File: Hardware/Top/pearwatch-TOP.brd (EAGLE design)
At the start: 38 x 38 mm, 49 parts, among them U2 NRF52832_MODULE_MDBT42, U4 PCF8523

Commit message: adding updated top board
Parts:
- added SW1, SW2: SWITCH.MOM, LinnesLab-Switches:TACTILE_SWITCH_SMD_6.2MM_TALL
- moved LDO2 9.76 mm to (9.45, 9.14)
- moved D5 7.69 mm to (3.38, 7.21)
- moved R15 7.57 mm to (17.8, 9.45)
- moved D4 7.44 mm to (3.45, 8.97)
- moved C6 7.39 mm to (15.8, 9.25)
- moved C5 5.79 mm to (12.5, 8.92), turned to 180 degrees
- moved R12 5.43 mm to (13.2, 10.3)
- moved C20 4.28 mm to (11.3, 12.7)
- moved R14 4.02 mm to (6.60, 8.43)
- moved CHRG2 3.69 mm to (14.8, 12.5)
- moved R13 1.58 mm to (8.94, 12.5)
- moved C21 1.49 mm to (19.6, 11.0)
- moved R11 1.42 mm to (18.5, 13.2)
- moved XTAL3 0.77 mm to (3.40, 29.4)
- moved R7 0.74 mm to (6.02, 10.7)
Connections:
- net GND: now also USB2.S1, USB2.S2, USB2.S3, USB2.S4, USB2.S5, USB2.S6
- net N$5: now also C14.2, D1.+, R5.1
- net RESET: no longer C14.2, D1.+, R5.1

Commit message: updating top board
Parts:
- removed C10, C11: 300p, LinnesLab-Passives:C0603
- removed C12: 10u, LinnesLab-Passives:C0805
- removed C13, C15, C17, C18, C19: 2.2uF, LinnesLab-Passives:C0402
- removed C14: 100n, LinnesLab-Passives:C0603
- removed C16: 10uF, LinnesLab-Passives:C0603
- removed CORTEX1: CORTEX_DEBUG_PTH, LinnesLab-Connectors:2X5-PTH-1.27MM
- removed D1: (no value), LinnesLab-DiscreteSemi:USC
- removed L2: 10u, LinnesLab-Passives:L0603
- removed SW3, SW4: (no value), LinnesLab-Switches:BUTTON-GULLWING
- removed U4: PCF8523, LinnesLab-Clocks:SO8
- removed XTAL3: 32.7680kHz, LinnesLab-Clocks:2-SMD.NOLEAD.2.0MMTO1.2MM
- added C25, C33, C35, C36, C37: 2.2uF, LinnesLab-Passives:C0402
- added C26: 1u, LinnesLab-Passives:C0603
- added C27, C28: (no value), LinnesLab-Passives:C0603
- added C29, C30: 300p, LinnesLab-Passives:C0603
- added C31: 10u, LinnesLab-Passives:C0805
- added C32: 100n, LinnesLab-Passives:C0603
- added C34: 10uF, LinnesLab-Passives:C0603
- added CORTEX3: CORTEX_DEBUG_PTH, LinnesLab-Connectors:2X5-PTH-1.27MM
- added D3: (no value), LinnesLab-DiscreteSemi:USC
- added JP2: (no value), LinnesLab-Switches:SMT-JUMPER_2_NO_SILK
- added L3: 10u, LinnesLab-Passives:L0603
- added LED5: RED, LinnesLab-LED:LED-0603
- added LED6: BLUE, LinnesLab-LED:LED-0603
- added R10, R18: 10k, LinnesLab-Passives:R0603
- added R16, R17, R20: 1k, LinnesLab-Passives:R0603
- added R19: 390k, LinnesLab-Passives:R0603
- added R21, R22: (no value), LinnesLab-Passives:R0603
- added SW7, SW8: (no value), LinnesLab-Switches:BUTTON-GULLWING
- added U5: NRF52832_MODULE_MDBT42, LinnesLab-Microcontrollers:BLE_MODULE_RAYTAC_MDBT42
- added U6: (no value), LinnesLab-Displays:UG-2864HSWEG01_0.96IN_NO-WRAPAROUND
- added XTAL4: 32.768kHz, LinnesLab-Clocks:2-SMD.NOLEAD.2.0MMTO1.2MM
- C7: value 1u -> 100n
- C8, C9: value (none) -> 47p
- LED4: value BLUE -> YELLOW
- R3, R4: value 1k -> 10k
- R5, R6: value 10k -> 27
- R7: value 390k -> 1k
- R8, R9: value 10k -> 10K
- U2: value NRF52832_MODULE_MDBT42 -> FT231XS; device LinnesLab-Microcontrollers:BLE_MODULE_RAYTAC_MDBT42 -> LinnesLab-DigitalIC:SSOP20_L
- U3: value (none) -> PCF8523; device LinnesLab-Displays:UG-2864HSWEG01_0.96IN_NO-WRAPAROUND -> LinnesLab-Clocks:SO8
- XTAL2: value 32.768kHz -> 32.7680kHz
- moved R7 72.8 mm to (77.6, -2.57)
- moved C7 54.1 mm to (73.8, 5.31), turned to 0 degrees
- moved C8 50.8 mm to (73.8, 0.23)
- moved C9 48.9 mm to (73.8, -4.85)
- moved LED4 43.7 mm to (77.6, 1.24)
- moved R5 41.2 mm to (6.27, 4.55), turned to 0 degrees
- moved LED3 40.5 mm to (77.6, 5.05)
- moved XTAL2 28.5 mm to (2.13, 30.6), turned to 90 degrees
- moved R8 27.0 mm to (29.5, 5.77), turned to 0 degrees
- moved R9 27.0 mm to (29.5, 3.07), turned to 0 degrees
- moved R4 25.9 mm to (13.4, 25.4), turned to 90 degrees
- moved R3 25.6 mm to (13.4, 28.8), turned to 90 degrees
- moved U3 14.7 mm to (3.68, 24.6)
- moved R6 10.4 mm to (5.46, 2.31)
- moved U2 9.84 mm to (21.5, 25.7), turned to 270 degrees
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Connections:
- removed net N$10: LED4.A, R4.1
- removed net N$11: L2.1, U2.10
- removed net N$12: C7.1, L2.2, U2.9
- removed net N$13: C16.2, U3.28
- removed net N$14: CORTEX1.8
- removed net N$15: C18.2, U3.27
- removed net N$19: U4.2, XTAL3.P$1
- removed net N$20: U4.1, XTAL3.P$2
- removed net N$4: C8.2, U2.13, XTAL2.P$1
- removed net N$5: C13.1, C14.2, D1.+, R5.1, U3.3
- removed net N$9: LED3.A, R3.1
- removed net RXD: U2.21
- removed net TXD: U2.19
- new net !CTS: JP2.2, U2.9
- new net !DTR: U2.1
- new net FT3V3: U2.13
- new net N$18: R10.2, U6.11
- new net N$21: R19.1, U6.26
- new net N$23: C25.2, U6.2
- new net N$26: C27.2, U5.13, XTAL4.P$1
- new net N$27: C28.1, U5.14, XTAL4.P$2
- new net N$28: LED5.A, R16.1
- new net N$29: LED6.A, R17.1
- new net N$30: L3.1, U5.10
- new net N$31: C26.1, L3.2, U5.9
- new net N$32: CORTEX3.8
- new net N$33: C25.1, U6.3
- new net N$34: C33.2, U6.4
- new net N$35: C33.1, U6.5
- new net N$36: C34.2, U6.28
- new net N$37: C36.2, U6.27
- new net RXD.FT: U2.4
- new net RXD.NRF: R21.2, U5.21
- new net RXDFT: R22.1
- new net RXLED: R7.1, U2.17
- new net TXD.FT: R21.1, U2.20
- new net TXD.NRF: R22.2, U5.19
- new net TXLED: R20.1, U2.10
- net 3.3V: now also C31.2, C35.2, C37.2, C7.2, CORTEX3.1, D3.-, LED3.A, LED4.A, R18.2, R3.2, R4.2, U2.14, U2.3, U3.8, U5.11, U6.6, U6.9; no longer C12.2, C17.2, C19.2, CORTEX1.1, D1.-, R5.2, U2.11, U3.6, U3.9, U4.8
- net CS.OLED: now also U6.13; no longer U3.13
- net DC.OLED: now also U6.15; no longer U3.15
- net DFU: now also SW7.3, U5.34; no longer SW3.3, U2.34
- net DTR: now also C32.1; no longer C14.1
- net FRST: now also U5.38; no longer U2.38
- net GND: now also C26.2, C27.1, C28.2, C29.2, C30.2, C31.1, C34.1, C35.1, C36.1, C37.1, C7.1, C8.2, C9.1, CORTEX3.3, CORTEX3.5, CORTEX3.7, CORTEX3.9, JP2.1, LED5.C, LED6.C, R10.1, R19.2, SW7.1, SW8.3, U2.16, U2.6, U3.4, U5.1, U5.12, U5.24, U5.39, U6.1, U6.10, U6.12, U6.29, U6.30, U6.8; no longer C10.2, C11.2, C12.1, C16.1, C17.1, C18.1, C19.1, C7.2, C8.1, C9.2, CORTEX1.3, CORTEX1.5, CORTEX1.7, CORTEX1.9, LED3.C, LED4.C, R6.1, R7.2, SW3.1, SW4.3, U2.1, U2.12, U2.24, U2.39, U3.1, U3.10, U3.12, U3.29, U3.30, U3.8, U4.4
- net LED1: now also R16.2, U5.31; no longer R3.2, U2.31
- net LED2: now also R17.2, U5.33; no longer R4.2, U2.33
- net MISO: now also U5.28; no longer U2.28
- net MOSI: now also U5.27, U6.19; no longer U2.27, U3.19
- net N$1: now also U3.2, XTAL2.P$1; no longer R6.2, U3.11
- net N$2: now also U3.1, XTAL2.P$2; no longer R7.1, U3.26
- net N$3: now also R5.2, U2.12; no longer C13.2, U3.2
- net N$6: now also R6.2, U2.11; no longer C9.1, U2.14, XTAL2.P$2
- net N$7: now also LED3.C, R7.2; no longer C15.2, U3.4
- net N$8: now also LED4.C, R20.2; no longer C15.1, U3.5
- net P0.09/NFC1: now also C30.1, U5.22; no longer C11.1, U2.22
- net P0.10/NFC2: now also C29.1, U5.23; no longer C10.1, U2.23
- net RESET: now also C32.2, CORTEX3.10, D3.+, R18.1, SW8.1, U5.35; no longer CORTEX1.10, SW4.1, U2.35
- net RESET.OLED: now also U6.14; no longer U3.14
- net SCK: now also U5.26, U6.18; no longer U2.26, U3.18
- net SCL: now also R3.1, R9.1, U3.6, U5.3; no longer R8.1, U2.3, U4.6
- net SDA: now also R4.1, R8.1, U3.5, U5.2; no longer R9.1, U2.2, U4.5
- net SWCLK: now also CORTEX3.4, U5.36; no longer CORTEX1.4, U2.36
- net SWDIO: now also CORTEX3.2, U5.37; no longer CORTEX1.2, U2.37
- net SWO: now also CORTEX3.6, U5.32; no longer CORTEX1.6, U2.32
- net USB+: now also C8.1, R6.1
- net USB-: now also C9.2, R5.1
- net VBATT: now also U3.3; no longer U4.3
- net V_USB: now also U2.15

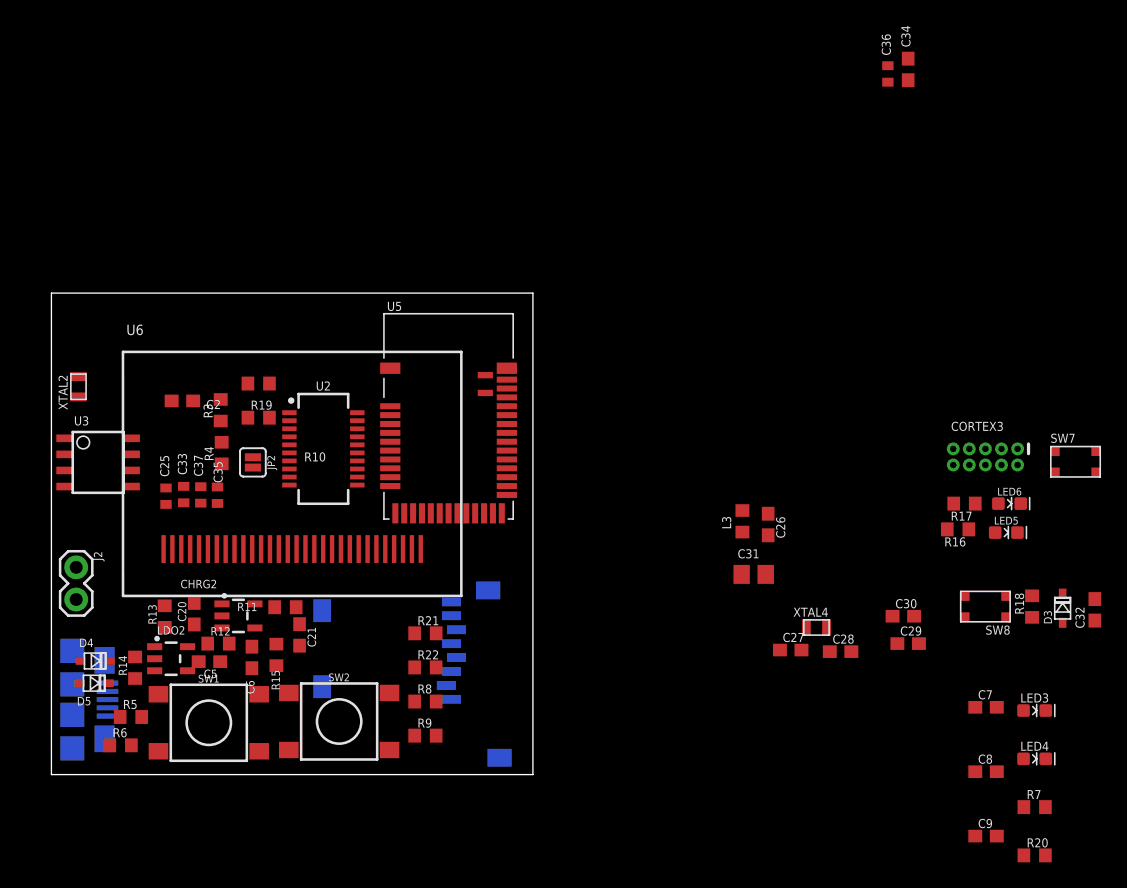
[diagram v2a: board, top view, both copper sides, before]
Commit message: deleted power management from top board
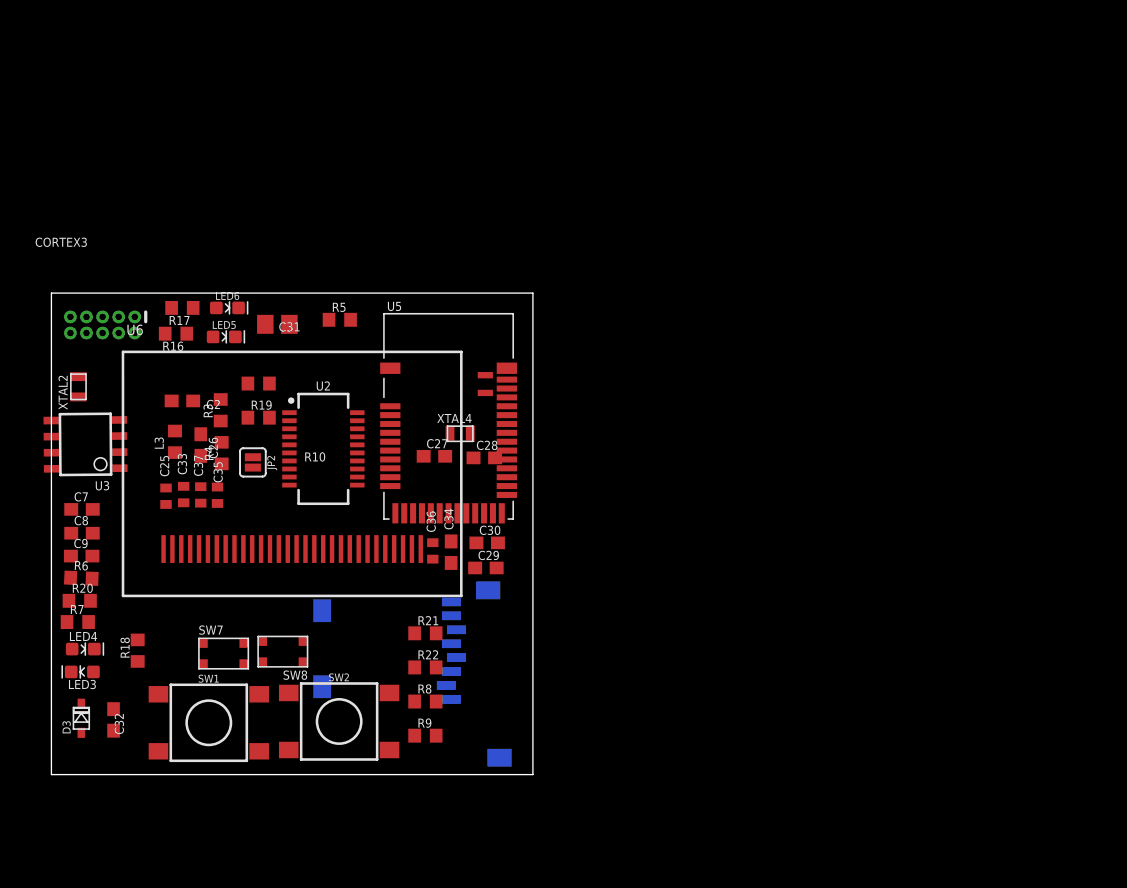
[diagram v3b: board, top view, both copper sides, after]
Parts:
- removed C20, C21: 4.7u, LinnesLab-Passives:C0603
- removed C5, C6: 1u, LinnesLab-Passives:C0603
- removed CHRG2: MCP73831, LinnesLab-Power:SOT23-5
- removed D4, D5: (no value), LinnesLab-DiscreteSemi:USC
- removed J2: (no value), LinnesLab-Connectors:1X02
- removed LDO2: MIC5504, LinnesLab-Power:SOT23-5
- removed R11: (no value), LinnesLab-Passives:R0603
- removed R12, R13, R14, R15: 100k, LinnesLab-Passives:R0603
- removed USB2: USB.MICRO-BIGGERPADS, LinnesLab-Connectors:USB-MICRO-01.BIGGERPADS
- moved R20 78.0 mm to (2.24, 13.7)
- moved C32 77.9 mm to (4.90, 4.32)
- moved D3 77.9 mm to (2.36, 4.45)
- moved R7 76.9 mm to (2.08, 12.0)
- moved LED4 75.6 mm to (2.51, 9.91)
- moved LED3 75.2 mm to (2.44, 8.10), turned to 180 degrees
- moved C9 74.7 mm to (2.39, 17.2)
- moved C8 73.8 mm to (2.41, 19.1)
- moved C7 73.0 mm to (2.41, 20.9)
- moved R18 70.7 mm to (6.81, 9.78)
- moved CORTEX3 70.4 mm to (4.04, 35.5)
- moved SW7 68.9 mm to (13.6, 9.55)
- moved LED5 63.6 mm to (13.6, 34.5)
- moved R16 63.6 mm to (9.83, 34.8)
- moved LED6 63.6 mm to (13.9, 36.8)
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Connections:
- removed net BATT: R13.1, R14.2
- removed net CHRG.STAT: CHRG2.1, R12.1
- removed net N$17: CHRG2.5, R11.2
- removed net VIN: C21.2, C5.2, CHRG2.4, D4.-, D5.-, LDO2.1, LDO2.3, R12.2
- removed net VLIPO: C20.1, CHRG2.3, D4.+, J2.2, R13.2
- net 3.3V: no longer C6.1, LDO2.5, R15.2
- net GND: no longer C20.2, C21.1, C5.1, C6.2, CHRG2.2, J2.1, LDO2.2, R11.1, R14.1, R15.1, USB2.5, USB2.S1, USB2.S2, USB2.S3, USB2.S4, USB2.S5, USB2.S6
- net USB+: no longer USB2.3
- net USB-: no longer USB2.2
- net V_USB: no longer D5.+, USB2.1

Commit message: making connections top and bottom board
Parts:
- added J1: (no value), LinnesLab-Connectors:1X07
- moved LED5 37.4 mm to (50.1, 26.1)
- moved LED6 37.4 mm to (50.3, 28.3)
- moved R16 37.4 mm to (46.3, 26.3)
- moved R17 37.4 mm to (46.8, 28.3)
- moved C26 25.8 mm to (10.7, 51.8)
- moved R3 25.8 mm to (12.2, 54.5)
- moved R4 25.8 mm to (12.3, 51.1)
- moved C2 25.8 mm to (9.22, 55.2)
- moved L3 25.8 mm to (8.64, 52.0)
- moved C37 0.84 mm to (12.6, 22.1), turned to 90 degrees
- moved C33 0.82 mm to (11.3, 22.2)
- moved C35 0.81 mm to (13.9, 22.0), turned to 90 degrees
- moved C25 0.77 mm to (9.80, 22.1)
- renumbered SW1 to D11/SW1, SW2 to D15/SW2
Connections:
- removed net DC.OLED: U6.15
- removed net RESET.OLED: U6.14
- removed net SD.CS: SD2.2
- new net A4/BATT: U5.5
- new net A6/TIA: U5.7
- new net A7/PPG: U5.8
- new net D11/SW1: U5.25
- new net D15/SW2: U5.29
- new net D27/CHRG.STATUS: U5.4
- new net D29/LED.CTRL: U5.6
- new net D3/RESET.OLED: U5.16, U6.14
- new net D4/DC.OLED: U5.17, U6.15
- new net D7/SD.CS: SD2.2, U5.20
